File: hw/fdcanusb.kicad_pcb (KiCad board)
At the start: 4 copper layers, 30 x 18 mm, 36 parts, among them J1 Conn_01x03, J2 216990-0002, J3 Conn_01x01, J4 Conn_01x01, J5 Conn_01x01, U1 STM32G474CEU6, U2 TCAN1057AEVDRQ1, U3 TLP3317, U4 USBLC6-2SC6, U5 TLV70233DSER

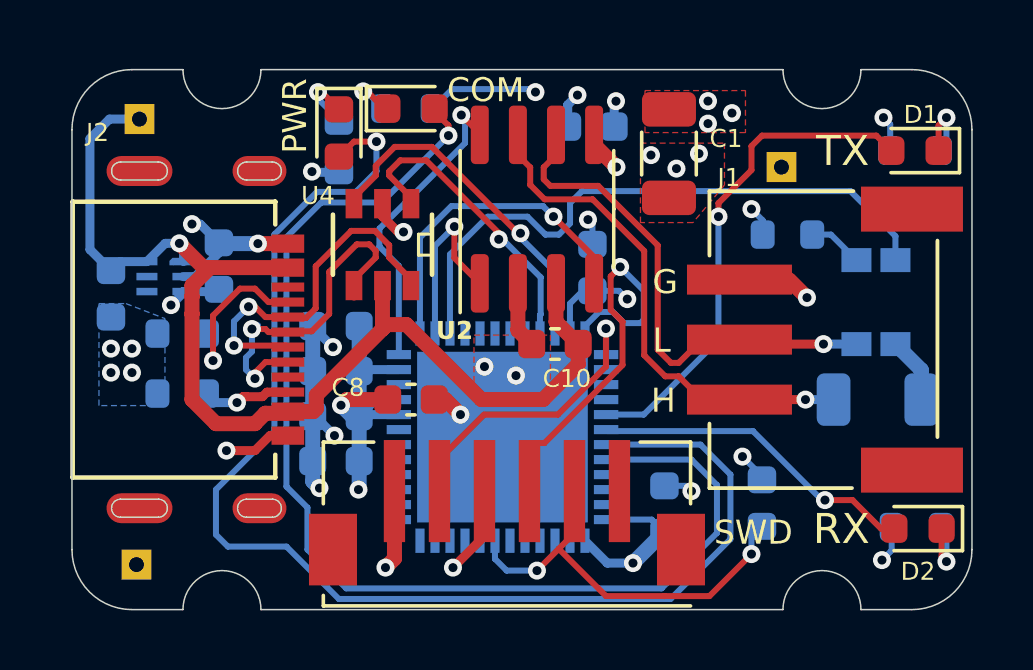
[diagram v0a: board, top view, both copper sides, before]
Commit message: r4.1: Swith to an actual SMT USB-C connector
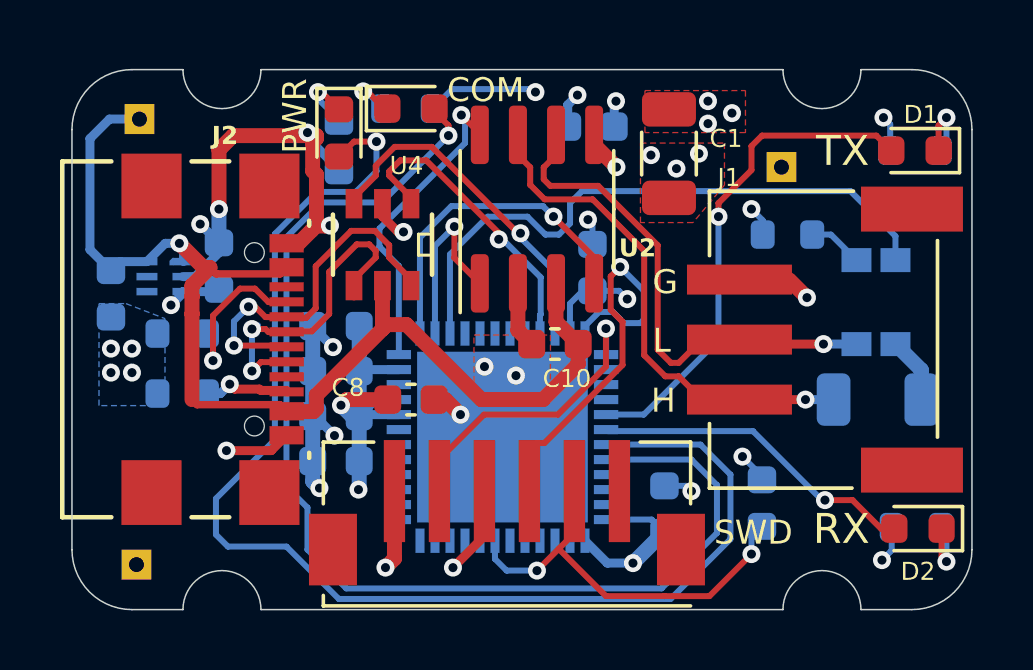
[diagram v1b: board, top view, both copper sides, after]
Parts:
- J2: value 216990-0002 -> USB4110-GF-A; footprint fdcanusb:216990-0002_MOL -> fdcanusb:USB4110-GF-A_GCT
- moved J2 0.39 mm to (123.8, 100.0)
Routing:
- net GND: track 36.7 -> 46.4 mm, vias 27 -> 28
- net /Power Input/USB_P: track 11.6 -> 11.0 mm
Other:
- board text added: "fdcanusb r4.1"
- board text removed: "fdcanusb r4"

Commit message: Rename board to mjcanfd-usb-1x
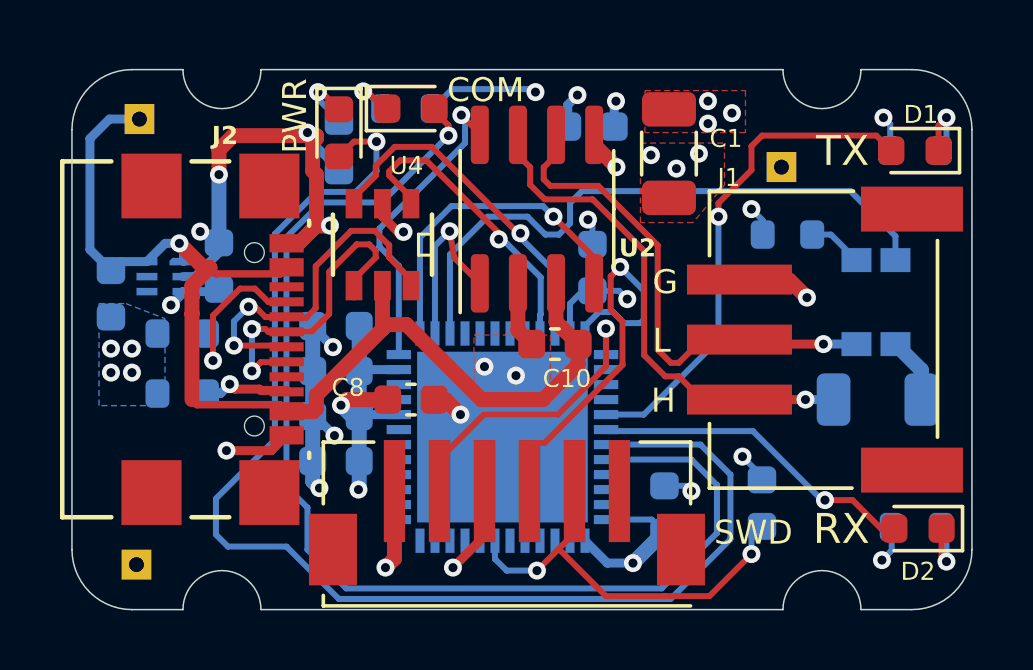
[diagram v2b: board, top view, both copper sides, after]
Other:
- board text added: "(c) 2024"
- board text added: "mjcanfd-usb-1x r4.1"
- board text removed: "(c) 2023"
- board text removed: "fdcanusb r4.1"
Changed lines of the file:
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@@
     (property "ki_keywords" "cap capacitor")
     (attr smd)
-    (fp_text reference "C13" (at -1.925 0 unlocked) (layer "B.SilkS")
+    (fp_text reference "C13" (at -1.925 0.2 unlocked) (layer "B.SilkS")
         (effects (font (size 0.6 0.6) (thickness 0.1)) (justify mirror))
     )
@@
     (property "ki_keywords" "TLV70233DSER")
     (attr smd)
-    (fp_text reference "U5" (at 0.100001 1.600001 unlocked) (layer "B.SilkS")
+    (fp_text reference "U5" (at 0.400001 1.400001 unlocked) (layer "B.SilkS")
         (effects (font (size 0.6 0.6) (thickness 0.1)) (justify mirror))
     )
@@
     (property "ki_keywords" "R res resistor")
     (attr smd)
-    (fp_text reference "R3" (at -2.325 -0.6 270 unlocked) (layer "B.SilkS")
-        (effects (font (size 0.5 0.5) (thickness 0.08)) (justify mirror))
+    (fp_text reference "R3" (at -2.347216 -0.565174 270 unlocked) (layer "B.SilkS")
+        (effects (font (size 0.45 0.45) (thickness 0.08)) (justify mirror))
     )
     (fp_text value "5.1k" (at 0 -1.43) (layer "B.Fab") hide
@@
     (effects (font (size 0.8 0.8) (thickness 0.125)) (justify left bottom mirror))
   )
-  (gr_text "(c) 2023" (at 133.7 97.75) (layer "B.SilkS")
+  (gr_text "(c) 2024" (at 133.7 97.75) (layer "B.SilkS")
     (effects (font (size 0.8 0.8) (thickness 0.125)) (justify left bottom mirror))
   )
-  (gr_text "fdcanusb r4.1" (at 133 96) (layer "B.SilkS")
+  (gr_text "mjcanfd-usb-1x r4.1" (at 133 96) (layer "B.SilkS")
     (effects (font (size 0.7 0.7) (thickness 0.125)) (justify left bottom mirror))
   )
@@
   (segment (start 134.865 98.125) (end 134.865 99.69) (width 0.5) (layer "F.Cu") (net 2))
   (segment (start 127.1973 103.200527) (end 127.144472 103.200527) (width 0.3) (layer "F.Cu") (net 2))
+  (segment (start 128.15 93.2) (end 128.15 93.296561) (width 0.5) (layer "F.Cu") (net 2))
   (segment (start 143.9 98) (end 144.5 98.6) (width 0.5) (layer "F.Cu") (net 2))
-  (segment (start 124.9 93.6724) (end 125.3724 93.2) (width 0.5) (layer "F.Cu") (net 2))
-  (segment (start 128.15 93.296561) (end 128.0226 93.423961) (width 0.5) (layer "F.Cu") (net 2))
-  (segment (start 124.9 95.65) (end 124.9 93.6724) (width 0.5) (layer "F.Cu") (net 2))
-  (segment (start 127.548025 96.799575) (end 127.1973 96.799575) (width 0.5) (layer "F.Cu") (net 2))
   (segment (start 125.3724 93.2) (end 128.15 93.2) (width 0.5) (layer "F.Cu") (net 2))
+  (segment (start 128.0226 94.376039) (end 128.15 94.503439) (width 0.5) (layer "F.Cu") (net 2))
+  (segment (start 127.548025 96.799575) (end 127.1973 96.799575) (width 0.5) (layer "F.Cu") (net 2))
   (segment (start 128.4381 96.3619) (end 128.6 96.2) (width 0.2) (layer "F.Cu") (net 2))
   (segment (start 132.45 102) (end 132.95 102.5) (width 0.5) (layer "F.Cu") (net 2))
@@
   (segment (start 130.349999 95.892649) (end 130.868902 96.411552) (width 0.3) (layer "F.Cu") (net 2))
   (segment (start 126.644999 103.7) (end 125.15 103.7) (width 0.3) (layer "F.Cu") (net 2))
-  (segment (start 128.15 93.2) (end 128.15 93.296561) (width 0.5) (layer "F.Cu") (net 2))
+  (segment (start 124.9 94.5) (end 124.9 93.6724) (width 0.5) (layer "F.Cu") (net 2))
   (segment (start 128.15 96.1976) (end 127.9857 96.3619) (width 0.5) (layer "F.Cu") (net 2))
   (segment (start 130.868902 96.411552) (end 131.0512 96.411552) (width 0.3) (layer "F.Cu") (net 2))
   (segment (start 127.9857 96.3619) (end 128.4381 96.3619) (width 0.2) (layer "F.Cu") (net 2))
+  (segment (start 128.0226 93.423961) (end 128.0226 94.376039) (width 0.5) (layer "F.Cu") (net 2))
   (segment (start 134.865 99.69) (end 135.325 100.15) (width 0.5) (layer "F.Cu") (net 2))
   (segment (start 133.749998 106.550002) (end 132.7 107.6) (width 0.3) (layer "F.Cu") (net 2))
-  (segment (start 128.0226 94.376039) (end 128.15 94.503439) (width 0.5) (layer "F.Cu") (net 2))
+  (segment (start 128.15 94.503439) (end 128.15 96.1976) (width 0.5) (layer "F.Cu") (net 2))
   (segment (start 133.749998 105.049999) (end 133.749998 106.550002) (width 0.3) (layer "F.Cu") (net 2))
   (segment (start 130.349999 95.4695) (end 130.349999 95.892649) (width 0.3) (layer "F.Cu") (net 2))
-  (segment (start 128.0226 93.423961) (end 128.0226 94.376039) (width 0.5) (layer "F.Cu") (net 2))
   (segment (start 132.075 102) (end 132.45 102) (width 0.5) (layer "F.Cu") (net 2))
   (segment (start 142.25 98) (end 143.9 98) (width 0.3) (layer "F.Cu") (net 2))
-  (segment (start 128.15 94.503439) (end 128.15 96.1976) (width 0.5) (layer "F.Cu") (net 2))
+  (segment (start 124.9 93.6724) (end 125.3724 93.2) (width 0.5) (layer "F.Cu") (net 2))
+  (segment (start 128.15 93.296561) (end 128.0226 93.423961) (width 0.5) (layer "F.Cu") (net 2))
   (segment (start 127.9857 96.3619) (end 127.548025 96.799575) (width 0.5) (layer "F.Cu") (net 2))
   (via (at 142.35 103.9) (size 0.6) (drill 0.3) (layers "F.Cu" "B.Cu") (net 2))
-  (via (at 124.9 95.65) (size 0.6) (drill 0.3) (layers "F.Cu" "B.Cu") (net 2))
+  (via (at 124.9 94.5) (size 0.6) (drill 0.3) (layers "F.Cu" "B.Cu") (net 2))
   (via (at 140.65 105.05) (size 0.6) (drill 0.3) (layers "F.Cu" "B.Cu") (net 2))
   (via (at 139.3 93.85) (size 0.6) (drill 0.3) (layers "F.Cu" "B.Cu") (free) (net 2))
@@
   (via (at 136.85 91.85) (size 0.6) (drill 0.3) (layers "F.Cu" "B.Cu") (net 2))
   (via (at 132.95 102.5) (size 0.6) (drill 0.3) (layers "F.Cu" "B.Cu") (net 2))
-  (via (at 124.275002 96.149999) (size 0.6) (drill 0.3) (layers "F.Cu" "B.Cu") (net 2))
+  (via (at 124.275002 96.4) (size 0.6) (drill 0.3) (layers "F.Cu" "B.Cu") (net 2))
   (via (at 134.8 101.2) (size 0.6) (drill 0.3) (layers "F.Cu" "B.Cu") (net 2))
   (via (at 137.2 96) (size 0.6) (drill 0.3) (layers "F.Cu" "B.Cu") (net 2))
@@
   (segment (start 128.025 102.55) (end 128.025 104.05) (width 0.5) (layer "B.Cu") (net 2))
   (segment (start 128.025 102.55) (end 128.1 102.55) (width 0.3) (layer "B.Cu") (net 2))
-  (segment (start 124.9 95.65) (end 124.9 96.775) (width 0.5) (layer "B.Cu") (net 2))
   (segment (start 132.025 92.3) (end 132.675 91.65) (width 0.2) (layer "B.Cu") (net 2))
   (segment (start 128.025 101.05) (end 128.025 102.55) (width 0.5) (layer "B.Cu") (net 2))
+  (segment (start 124.275002 96.4) (end 124.9 96.775) (width 0.3) (layer "B.Cu") (net 2))
   (segment (start 128.025 99.575) (end 128.7 100.25) (width 0.3) (layer "B.Cu") (net 2))
-  (segment (start 124.275002 96.150002) (end 124.275002 96.149999) (width 0.3) (layer "B.Cu") (net 2))
   (segment (start 124.9 97.104144) (end 124.9 96.775) (width 0.3) (layer "B.Cu") (net 2))
   (segment (start 140.475 104.875) (end 140.65 105.05) (width 0.2) (layer "B.Cu") (net 2))
@@
   (segment (start 143 104.675) (end 143 104.55) (width 0.2) (layer "B.Cu") (net 2))
   (segment (start 132.200483 92.124517) (end 132.025 92.3) (width 0.3) (layer "B.Cu") (net 2))
-  (segment (start 124.9 96.775) (end 124.275002 96.150002) (width 0.3) (layer "B.Cu") (net 2))
   (segment (start 147.275 92.825) (end 147.05 92.6) (width 0.2) (layer "B.Cu") (net 2))
   (segment (start 139.75 104.875) (end 140.475 104.875) (width 0.2) (layer "B.Cu") (net 2))
+  (segment (start 124.9 94.5) (end 124.9 96.775) (width 0.5) (layer "B.Cu") (net 2))
   (segment (start 128.025 104.725) (end 128.25 104.95) (width 0.5) (layer "B.Cu") (net 2))
   (segment (start 143 104.55) (end 142.35 103.9) (width 0.2) (layer "B.Cu") (net 2))
@@
   (segment (start 135.7 95.55) (end 136.05 95.9) (width 0.2) (layer "B.Cu") (net 41))
   (segment (start 131.6 99.7956) (end 131.6 96.598368) (width 0.2) (layer "B.Cu") (net 41))
-  (segment (start 133.595 98.125) (end 132.746452 97.276452) (width 0.2) (layer "F.Cu") (net 42))
-  (segment (start 132.746452 97.276452) (end 132.746452 96.233128) (width 0.2) (layer "F.Cu") (net 42))
-  (via (at 132.746452 96.233128) (size 0.6) (drill 0.3) (layers "F.Cu" "B.Cu") (net 42))
-  (segment (start 132.099999 96.879581) (end 132.746452 96.233128) (width 0.2) (layer "B.Cu") (net 42))
-  (segment (start 132.099999 99.7956) (end 132.099999 96.879581) (width 0.2) (layer "B.Cu") (net 42))
+  (segment (start 132.746452 97.276452) (end 133.595 98.125) (width 0.2) (layer "F.Cu") (net 42))
+  (segment (start 132.58979 96.38979) (end 132.746452 97.276452) (width 0.2) (layer "F.Cu") (net 42))
+  (via (at 132.58979 96.38979) (size 0.6) (drill 0.3) (layers "F.Cu" "B.Cu") (net 42))
+  (segment (start 132.58979 96.38979) (end 132.099999 96.879581) (width 0.2) (layer "B.Cu") (net 42))
+  (segment (start 132.099999 96.879581) (end 132.099999 99.7956) (width 0.2) (layer "B.Cu") (net 42))
   (segment (start 132.600001 97.160791) (end 133.858392 95.9024) (width 0.2) (layer "B.Cu") (net 43))
   (segment (start 136.231212 96.5) (end 136.6024 96.128812) (width 0.2) (layer "B.Cu") (net 43))

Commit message: Add title block and update rev to r4.2
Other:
- board text added: "mjcanfd-usb-1x r4.2"
- board text removed: "mjcanfd-usb-1x r4.1"
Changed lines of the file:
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@@
     (effects (font (size 0.8 0.8) (thickness 0.125)) (justify left bottom mirror))
   )
-  (gr_text "mjcanfd-usb-1x r4.1" (at 133 96) (layer "B.SilkS")
+  (gr_text "mjcanfd-usb-1x r4.2" (at 133 96) (layer "B.SilkS")
     (effects (font (size 0.7 0.7) (thickness 0.125)) (justify left bottom mirror))
   )
